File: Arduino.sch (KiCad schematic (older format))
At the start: 16 parts

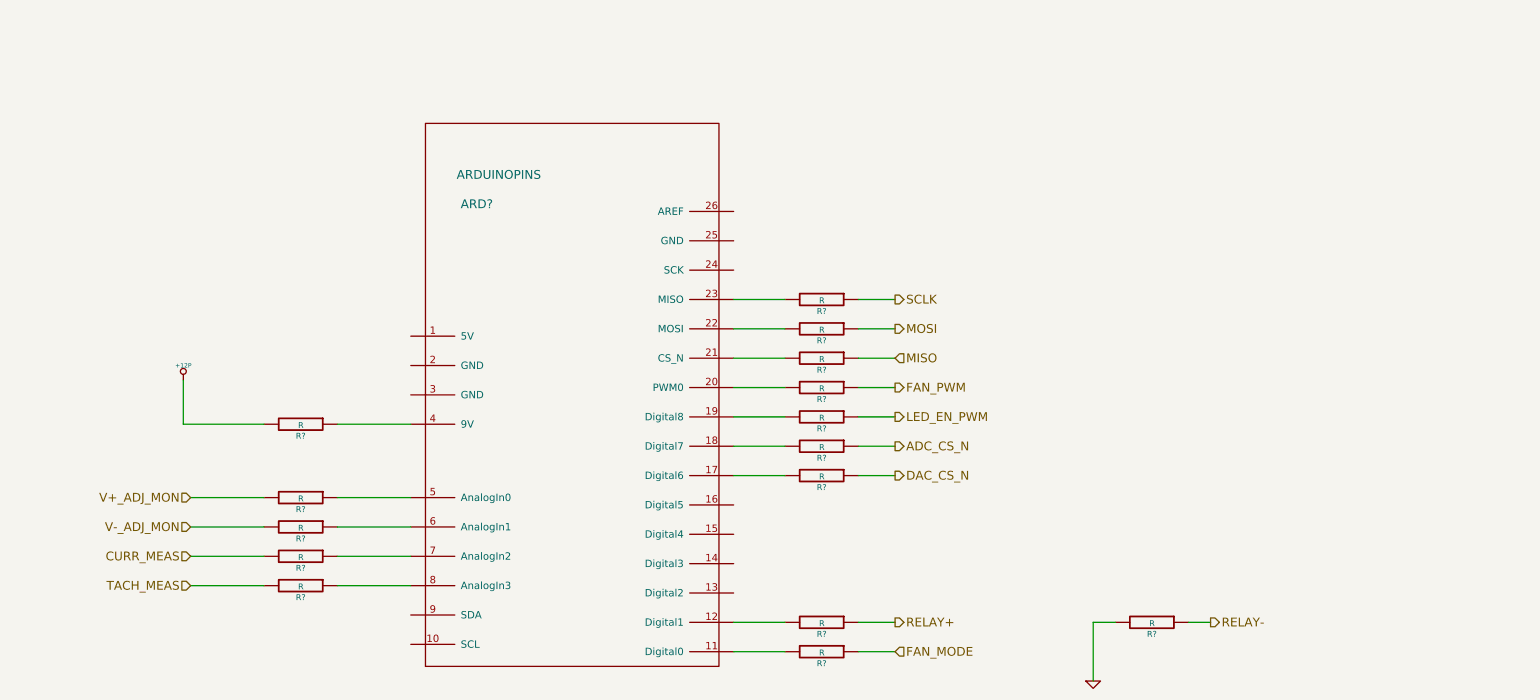
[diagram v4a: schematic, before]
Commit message: Clean Up Arduino Module
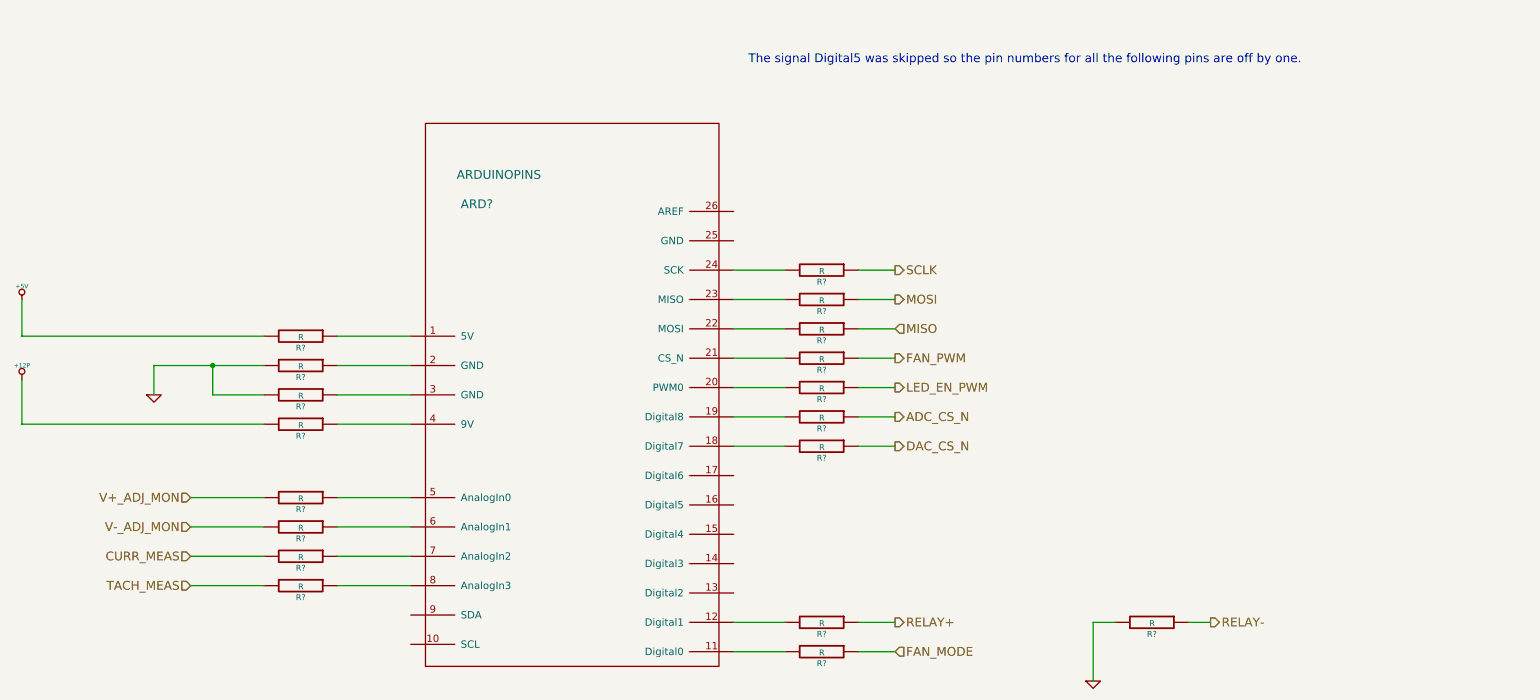
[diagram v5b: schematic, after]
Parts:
- removed ARD?: ARDUINOPINS, symbol ARDUINOPINS
- added ARD?: ARDUINOPINS, ~, symbol ARDUINOPINS
- added R? (x3): R, ~, symbol R
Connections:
- net GND: now also R?.2, R?.2
- net at R?.2: now also ARD?.11 (Digital0)
- net at R?.2: now also ARD?.12 (Digital1)
- net at R?.2: now also ARD?.18 (Digital7)
- net at R?.2: now also ARD?.19 (Digital8)
- net at R?.2: now also ARD?.20 (PWM0)
- net at R?.2: now also ARD?.21 (CS_N)
- net at R?.2: now also ARD?.22 (MOSI)
- net at R?.2: now also ARD?.23 (MISO)
- net at R?.2: now also ARD?.24 (SCK)
- net at R?.1: now also ARD?.4 (9V)
- net at R?.1: now also ARD?.5 (AnalogIn0)
- net at R?.1: now also ARD?.6 (AnalogIn1)
- net at R?.1: now also ARD?.7 (AnalogIn2)
- net at R?.1: now also ARD?.8 (AnalogIn3)
- new net: ARD?.1 (5V), R?.1
- new net: ARD?.2 (GND), R?.1
- new net: ARD?.3 (GND), R?.1
- new net +5V: R?.2
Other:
- note added: "The signal Digital5 was skipped so the pin numbers for all the following pins are off by one."
- moved on the sheet: R?
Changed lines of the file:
@@
-EESchema Schematic File Version 2  date 9/25/2013 9:42:53 PM
+EESchema Schematic File Version 2  date 10/6/2013 4:17:57 PM
 LIBS:power
 LIBS:device
@@
 Sheet 9 9
 Title ""
-Date "26 sep 2013"
+Date "6 oct 2013"
 Rev ""
 Comp ""
@@
 Text HLabel 9300 5700 2    60   Output ~ 0
 RELAY-
-Text HLabel 7150 3700 2    60   Output ~ 0
+Text HLabel 7150 3500 2    60   Output ~ 0
 MOSI
-Text HLabel 7150 3900 2    60   Input ~ 0
+Text HLabel 7150 3700 2    60   Input ~ 0
 MISO
-Text HLabel 7150 3500 2    60   Output ~ 0
+Text HLabel 7150 3300 2    60   Output ~ 0
 SCLK
-Text HLabel 7150 4700 2    60   Output ~ 0
+Text HLabel 7150 4500 2    60   Output ~ 0
 DAC_CS_N
-Text HLabel 7150 4100 2    60   Output ~ 0
+Text HLabel 7150 3900 2    60   Output ~ 0
 FAN_PWM
 Text HLabel 2350 5450 0    60   Input ~ 0
 TACH_MEAS
-$Comp
-L ARDUINOPINS ARD?
-U 1 1 524006C0
-P 4950 4450
-F 0 "ARD?" H 4300 6050 60  0000 C CNN
-F 1 "ARDUINOPINS" H 4450 6250 60  0000 C CNN
-F 2 "" H 5500 3500 60  0000 C CNN
-F 3 "" H 5500 3500 60  0000 C CNN
-	1    4950 4450
-	1    0    0    -1
-$EndComp
 Text HLabel 2350 5250 0    60   Input ~ 0
 CURR_MEAS
@@
 L R R?
 U 1 1 52400F4A
-P 6650 4100
-F 0 "R?" V 6730 4100 40  0000 C CNN
-F 1 "R" V 6657 4101 40  0000 C CNN
-F 2 "~" V 6580 4100 30  0000 C CNN
-F 3 "~" H 6650 4100 30  0000 C CNN
-	1    6650 4100
-	0    1    1    0
-$EndComp
-Wire Wire Line
-	7150 4100 6900 4100
-Wire Wire Line
-	6400 4100 6050 4100
+P 6650 3900
+F 0 "R?" V 6730 3900 40  0000 C CNN
+F 1 "R" V 6657 3901 40  0000 C CNN
+F 2 "~" V 6580 3900 30  0000 C CNN
+F 3 "~" H 6650 3900 30  0000 C CNN
+	1    6650 3900
+	0    1    1    0
+$EndComp
+Wire Wire Line
+	7150 3900 6900 3900
+Wire Wire Line
+	6400 3900 6050 3900
 $Comp
 L R R?
@@
 L R R?
 U 1 1 52402D2F
+P 6650 3300
+F 0 "R?" V 6730 3300 40  0000 C CNN
+F 1 "R" V 6657 3301 40  0000 C CNN
+F 2 "~" V 6580 3300 30  0000 C CNN
+F 3 "~" H 6650 3300 30  0000 C CNN
+	1    6650 3300
+	0    1    1    0
+$EndComp
+$Comp
+L R R?
+U 1 1 52402D35
 P 6650 3500
 F 0 "R?" V 6730 3500 40  0000 C CNN
@@
 $Comp
 L R R?
-U 1 1 52402D35
+U 1 1 52402D3B
 P 6650 3700
 F 0 "R?" V 6730 3700 40  0000 C CNN
@@
 $Comp
 L R R?
-U 1 1 52402D3B
-P 6650 3900
-F 0 "R?" V 6730 3900 40  0000 C CNN
-F 1 "R" V 6657 3901 40  0000 C CNN
-F 2 "~" V 6580 3900 30  0000 C CNN
-F 3 "~" H 6650 3900 30  0000 C CNN
-	1    6650 3900
-	0    1    1    0
-$EndComp
-$Comp
-L R R?
 U 1 1 52402D41
-P 6650 4700
-F 0 "R?" V 6730 4700 40  0000 C CNN
-F 1 "R" V 6657 4701 40  0000 C CNN
-F 2 "~" V 6580 4700 30  0000 C CNN
-F 3 "~" H 6650 4700 30  0000 C CNN
-	1    6650 4700
-	0    1    1    0
-$EndComp
+P 6650 4500
+F 0 "R?" V 6730 4500 40  0000 C CNN
+F 1 "R" V 6657 4501 40  0000 C CNN
+F 2 "~" V 6580 4500 30  0000 C CNN
+F 3 "~" H 6650 4500 30  0000 C CNN
+	1    6650 4500
+	0    1    1    0
+$EndComp
+Wire Wire Line
+	6400 3300 6050 3300
+Wire Wire Line
+	6900 3300 7150 3300
+Wire Wire Line
+	6900 3500 7150 3500
 Wire Wire Line
 	6400 3500 6050 3500
 Wire Wire Line
-	6900 3500 7150 3500
+	6400 3700 6050 3700
 Wire Wire Line
 	6900 3700 7150 3700
 Wire Wire Line
-	6400 3700 6050 3700
-Wire Wire Line
-	6400 3900 6050 3900
-Wire Wire Line
-	6900 3900 7150 3900
-Wire Wire Line
-	7150 4700 6900 4700
-Wire Wire Line
-	6400 4700 6050 4700
+	7150 4500 6900 4500
+Wire Wire Line
+	6400 4500 6050 4500
 $Comp
 L R R?
@@
 Wire Wire Line
 	9150 5700 9300 5700
-Text HLabel 7150 4300 2    60   Output ~ 0
+Text HLabel 7150 4100 2    60   Output ~ 0
 LED_EN_PWM
 $Comp
 L R R?
 U 1 1 52402E11
+P 6650 4100
+F 0 "R?" V 6730 4100 40  0000 C CNN
+F 1 "R" V 6657 4101 40  0000 C CNN
+F 2 "~" V 6580 4100 30  0000 C CNN
+F 3 "~" H 6650 4100 30  0000 C CNN
+	1    6650 4100
+	0    1    1    0
+$EndComp
+Wire Wire Line
+	6900 4100 7150 4100
+Wire Wire Line
+	6400 4100 6050 4100
+$Comp
+L R R?
+U 1 1 5240769E
 P 6650 4300
 F 0 "R?" V 6730 4300 40  0000 C CNN
@@
 $EndComp
 Wire Wire Line
-	6900 4300 7150 4300
-Wire Wire Line
 	6400 4300 6050 4300
-$Comp
-L R R?
-U 1 1 5240769E
-P 6650 4500
-F 0 "R?" V 6730 4500 40  0000 C CNN
-F 1 "R" V 6657 4501 40  0000 C CNN
-F 2 "~" V 6580 4500 30  0000 C CNN
-F 3 "~" H 6650 4500 30  0000 C CNN
-	1    6650 4500
-	0    1    1    0
-$EndComp
-Wire Wire Line
-	6400 4500 6050 4500
-Text HLabel 7150 4500 2    60   Output ~ 0
+Text HLabel 7150 4300 2    60   Output ~ 0
 ADC_CS_N
 Wire Wire Line
-	7150 4500 6900 4500
+	7150 4300 6900 4300
 Text HLabel 7150 5900 2    60   Input ~ 0
 FAN_MODE
@@
 L +12P #PWR?
 U 1 1 5243CFCD
-P 2300 4050
-F 0 "#PWR?" H 2300 4020 30  0001 C CNN
-F 1 "+12P" H 2300 4150 30  0000 C CNN
-F 2 "~" H 2300 4050 60  0000 C CNN
-F 3 "~" H 2300 4050 60  0000 C CNN
-	1    2300 4050
+P 1200 4050
+F 0 "#PWR?" H 1200 4020 30  0001 C CNN
+F 1 "+12P" H 1200 4150 30  0000 C CNN
+F 2 "~" H 1200 4050 60  0000 C CNN
+F 3 "~" H 1200 4050 60  0000 C CNN
+	1    1200 4050
 	1    0    0    -1
 $EndComp
 Wire Wire Line
-	2300 4050 2300 4350
-Wire Wire Line
-	2300 4350 2850 4350
+	1200 4050 1200 4350
+Wire Wire Line
+	1200 4350 2850 4350
+$Comp
+L R R?
+U 1 1 5245171E
+P 3100 3750
+F 0 "R?" V 3180 3750 40  0000 C CNN
+F 1 "R" V 3107 3751 40  0000 C CNN
+F 2 "~" V 3030 3750 30  0000 C CNN
+F 3 "~" H 3100 3750 30  0000 C CNN
+	1    3100 3750
+	0    1    1    0
+$EndComp
+Wire Wire Line
+	3350 3750 3850 3750
+$Comp
+L +5V #PWR?
+U 1 1 5245176C
+P 1200 3500
+F 0 "#PWR?" H 1200 3590 20  0001 C CNN
+F 1 "+5V" H 1200 3590 30  0000 C CNN
+F 2 "~" H 1200 3500 60  0000 C CNN
+F 3 "~" H 1200 3500 60  0000 C CNN
+	1    1200 3500
+	1    0    0    -1
+$EndComp
+Wire Wire Line
+	2850 3750 1200 3750
+Wire Wire Line
+	1200 3750 1200 3500
+Wire Wire Line
+	3850 3950 3350 3950
+$Comp
+L R R?
+U 1 1 524517C0
+P 3100 3950
+F 0 "R?" V 3180 3950 40  0000 C CNN
+F 1 "R" V 3107 3951 40  0000 C CNN
+F 2 "~" V 3030 3950 30  0000 C CNN
+F 3 "~" H 3100 3950 30  0000 C CNN
+	1    3100 3950
+	0    1    1    0
+$EndComp
+$Comp
+L R R?
+U 1 1 524517C6
+P 3100 4150
+F 0 "R?" V 3180 4150 40  0000 C CNN
+F 1 "R" V 3107 4151 40  0000 C CNN
+F 2 "~" V 3030 4150 30  0000 C CNN
+F 3 "~" H 3100 4150 30  0000 C CNN
+	1    3100 4150
+	0    1    1    0
+$EndComp
+Wire Wire Line
+	3350 4150 3850 4150
+Wire Wire Line
+	2850 3950 2100 3950
+Wire Wire Line
+	2100 3950 2100 4150
+$Comp
+L GND #PWR?
+U 1 1 5245181B
+P 2100 4150
+F 0 "#PWR?" H 2100 4150 30  0001 C CNN
+F 1 "GND" H 2100 4080 30  0001 C CNN
+F 2 "~" H 2100 4150 60  0000 C CNN
+F 3 "~" H 2100 4150 60  0000 C CNN
+	1    2100 4150
+	1    0    0    -1
+$EndComp
+Wire Wire Line
+	2850 4150 2500 4150
+Wire Wire Line
+	2500 4150 2500 3950
+Connection ~ 2500 3950
+Text Notes 6150 1900 0    60   ~ 0
+The signal Digital5 was skipped so the pin numbers for all the following pins are off by one.
+$Comp
+L ARDUINOPINS ARD?
+U 1 1 5251D4C8
+P 4950 4450
+F 0 "ARD?" H 4300 6050 60  0000 C CNN
+F 1 "ARDUINOPINS" H 4450 6250 60  0000 C CNN
+F 2 "~" H 5500 3500 60  0000 C CNN
+F 3 "~" H 5500 3500 60  0000 C CNN
+	1    4950 4450
+	1    0    0    -1
+$EndComp
 $EndSCHEMATC
